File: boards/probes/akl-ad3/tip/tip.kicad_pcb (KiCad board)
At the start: 2 copper layers, 44.5 x 25.5 mm, 11 parts, among them J1 Conn_01x10_shielded, J2 SOCKET, J3 SOCKET

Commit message: v0.2 AKL-AD3 tip
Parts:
- removed the REF** at (118.5, 54.5)
- added REF**: MECHANICAL_CLEARANCEHOLE_M1_UNPLATED, azonenberg_pcb:MECHANICAL_CLEARANCEHOLE_M1_UNPLATED, F.Cu at (118.5, 79.5)
- added REF**: MECHANICAL_CLEARANCEHOLE_M1_UNPLATED, azonenberg_pcb:MECHANICAL_CLEARANCEHOLE_M1_UNPLATED, F.Cu at (118.5, 52.5)
- added REF**: MECHANICAL_CLEARANCEHOLE_M1_UNPLATED, azonenberg_pcb:MECHANICAL_CLEARANCEHOLE_M1_UNPLATED, F.Cu at (120.5, 52.5)
- moved REF** 2.83 mm to (120.5, 79.5)
- moved J2 2.24 mm to (123.2, 52.9)
- moved J3 2.24 mm to (123.2, 79.2)
- moved R1 2.24 mm to (118.8, 54.0)
- moved R2 2.24 mm to (118.8, 78.0)
- moved R3 2.24 mm to (119.8, 54.0)
- moved R4 2.24 mm to (119.8, 78.0)
- moved R5 2.24 mm to (121.0, 54.0)
- moved R6 2.24 mm to (121.0, 78.0)
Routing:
- net /GND: track 195.4 -> 207.4 mm, vias 176 -> 188
- net /IN_R_N: track 48.6 -> 52.1 mm
- net /IN_R_P: track 48.7 -> 51.7 mm
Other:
- board size 44.5 x 25.5 mm -> 45.5 x 29.5 mm
- board text added: "v0.2"
- board text removed: "v0.1"

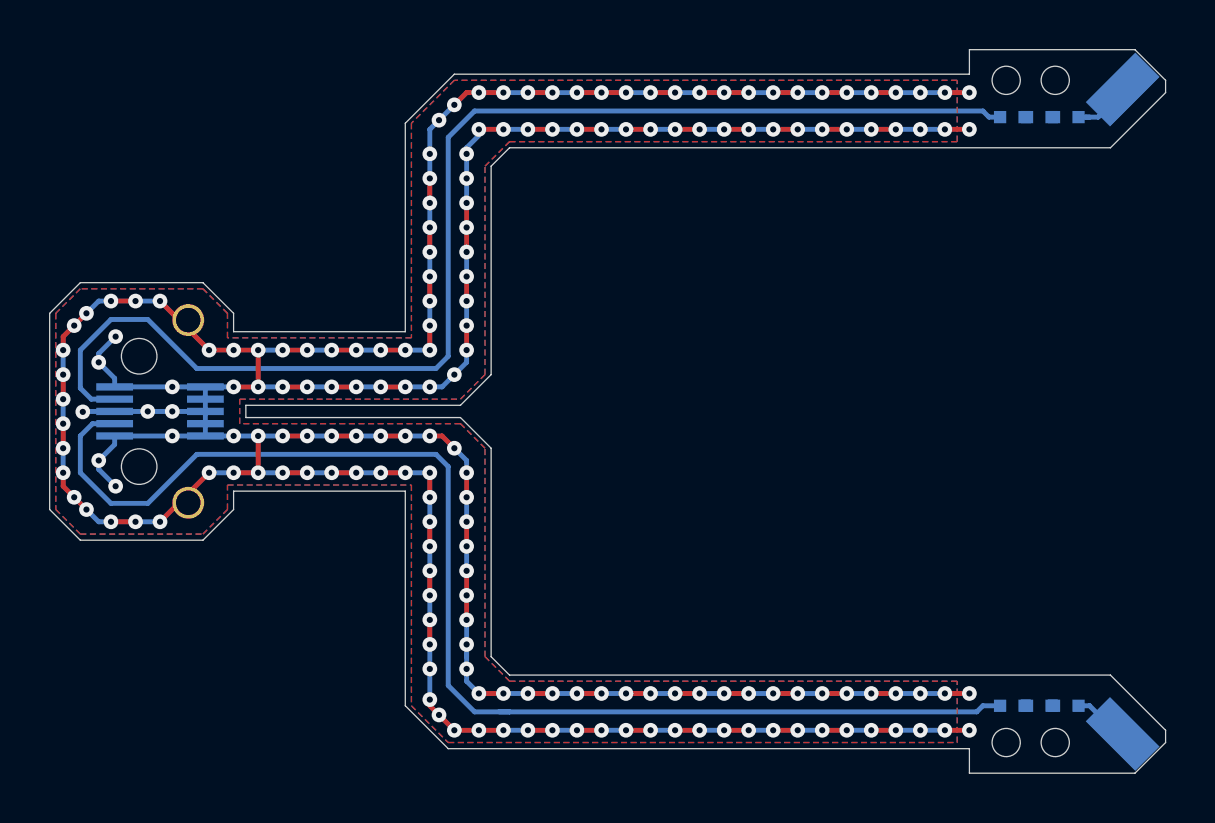
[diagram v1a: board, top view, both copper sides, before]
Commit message: Updated tip with correct copper pours. Bumped version number to v0.3 to disambiguate some mistyped numbers before.
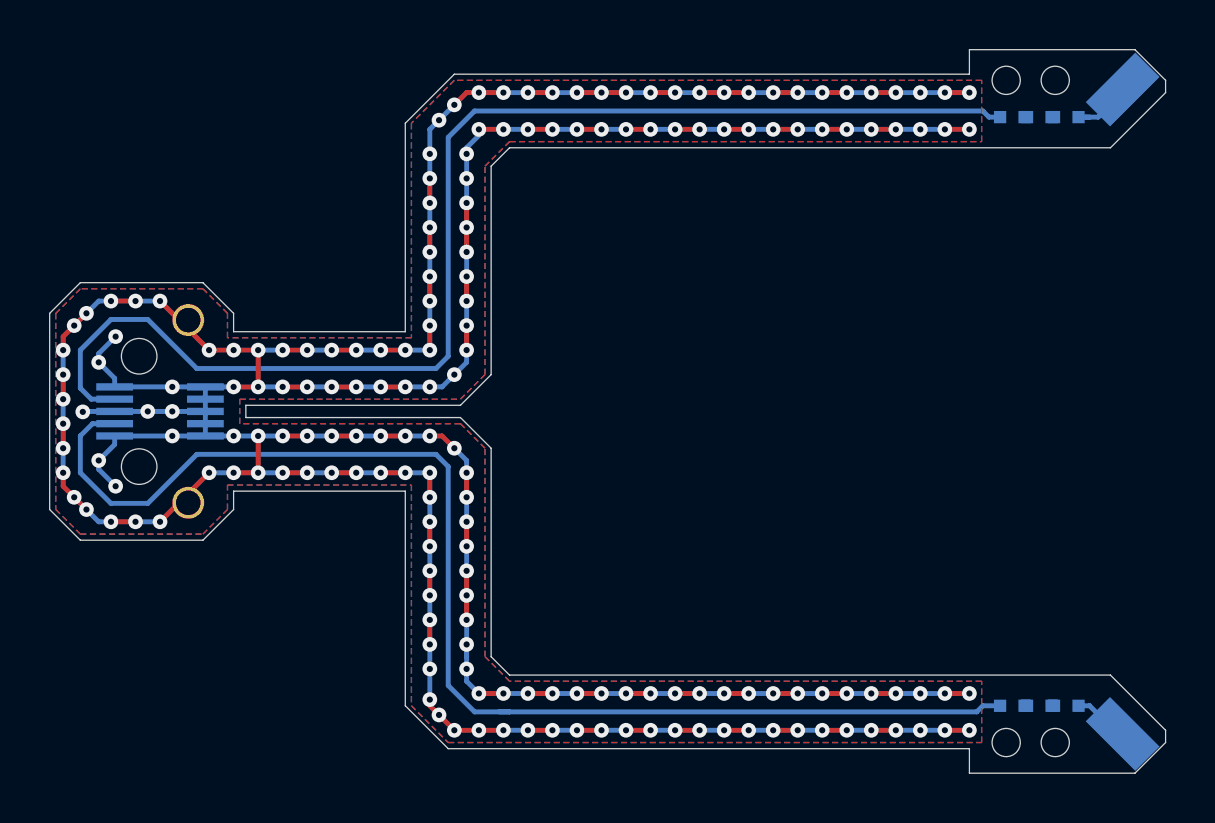
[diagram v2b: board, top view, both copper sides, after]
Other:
- board text added: "v0.3"
- board text removed: "v0.2"
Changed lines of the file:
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@@
     (effects (font (size 0.75 0.75) (thickness 0.1)) (justify mirror))
   )
-  (gr_text v0.2 (at 82.75 62.25) (layer B.SilkS)
+  (gr_text v0.3 (at 82.75 62.25) (layer B.SilkS)
     (effects (font (size 0.75 0.75) (thickness 0.1)) (justify mirror))
   )
@@
         (xy 80.75 61) (xy 79.75 62) (xy 79.75 70) (xy 80.75 71) (xy 85.75 71)
         (xy 86.75 70) (xy 86.75 69) (xy 94.25 69) (xy 94.25 78) (xy 95.75 79.5)
-        (xy 116.5 79.5) (xy 116.5 77) (xy 98.25 77) (xy 97.25 76) (xy 97.25 67.5)
+        (xy 117.5 79.5) (xy 117.5 77) (xy 98.25 77) (xy 97.25 76) (xy 97.25 67.5)
         (xy 96.25 66.5) (xy 87.25 66.5) (xy 87.25 65.5) (xy 96.25 65.5) (xy 97.25 64.5)
-        (xy 97.25 56) (xy 98.25 55) (xy 116.5 55) (xy 116.5 52.5) (xy 96 52.5)
+        (xy 97.25 56) (xy 98.25 55) (xy 117.5 55) (xy 117.5 52.5) (xy 96 52.5)
         (xy 94.25 54.25) (xy 94.25 63) (xy 86.75 63) (xy 86.75 62) (xy 85.75 61)
       )
@@
         (xy 80.75 61) (xy 79.75 62) (xy 79.75 70) (xy 80.75 71) (xy 85.75 71)
         (xy 86.75 70) (xy 86.75 69) (xy 94.25 69) (xy 94.25 78) (xy 95.75 79.5)
-        (xy 116.5 79.5) (xy 116.5 77) (xy 98.25 77) (xy 97.25 76) (xy 97.25 67.5)
+        (xy 117.5 79.5) (xy 117.5 77) (xy 98.25 77) (xy 97.25 76) (xy 97.25 67.5)
         (xy 96.25 66.5) (xy 87.25 66.5) (xy 87.25 65.5) (xy 96.25 65.5) (xy 97.25 64.5)
-        (xy 97.25 56) (xy 98.25 55) (xy 116.5 55) (xy 116.5 52.5) (xy 96 52.5)
+        (xy 97.25 56) (xy 98.25 55) (xy 117.5 55) (xy 117.5 52.5) (xy 96 52.5)
         (xy 94.25 54.25) (xy 94.25 63) (xy 86.75 63) (xy 86.75 62) (xy 85.75 61)
       )

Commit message: Missing change from last commit
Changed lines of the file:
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@@
     (thickness 0.2)
     (drawings 40)
-    (tracks 446)
+    (tracks 444)
     (zones 0)
     (modules 13)
@@
   (segment (start 82 62.25) (end 83.5 62.25) (width 0.2) (layer B.Cu) (net 3))
   (segment (start 117.55 78) (end 118.25 78) (width 0.2) (layer B.Cu) (net 5))
+  (segment (start 96.824998 78.25) (end 117.3 78.25) (width 0.2) (layer B.Cu) (net 5))
+  (segment (start 95.75 77.175002) (end 96.824998 78.25) (width 0.2) (layer B.Cu) (net 5))
+  (segment (start 95.25 67.75) (end 95.75 68.25) (width 0.2) (layer B.Cu) (net 5))
   (segment (start 117.3 78.25) (end 117.55 78) (width 0.2) (layer B.Cu) (net 5))
-  (segment (start 96.824998 78.25) (end 98.25 78.25) (width 0.2) (layer B.Cu) (net 5))
-  (segment (start 95.75 77.175002) (end 96.824998 78.25) (width 0.2) (layer B.Cu) (net 5))
   (segment (start 85.5 67.75) (end 95.25 67.75) (width 0.2) (layer B.Cu) (net 5))
   (segment (start 82 69.75) (end 83.5 69.75) (width 0.2) (layer B.Cu) (net 5))
-  (segment (start 95.25 67.75) (end 95.75 68.25) (width 0.2) (layer B.Cu) (net 5))
-  (segment (start 83.5 69.75) (end 85.5 67.75) (width 0.2) (layer B.Cu) (net 5))
-  (segment (start 98.25 78.25) (end 117.3 78.25) (width 0.2) (layer B.Cu) (net 5))
-  (segment (start 97.824998 78.25) (end 98.25 78.25) (width 0.2) (layer B.Cu) (net 5))
   (segment (start 82.15 66.5) (end 81.25 66.5) (width 0.2) (layer B.Cu) (net 5))
   (segment (start 95.75 68.25) (end 95.75 77.175002) (width 0.2) (layer B.Cu) (net 5))
+  (segment (start 80.75 67) (end 80.75 68.5) (width 0.2) (layer B.Cu) (net 5))
   (segment (start 81.25 66.5) (end 80.75 67) (width 0.2) (layer B.Cu) (net 5))
-  (segment (start 80.75 67) (end 80.75 68.5) (width 0.2) (layer B.Cu) (net 5))
   (segment (start 80.75 68.5) (end 82 69.75) (width 0.2) (layer B.Cu) (net 5))
+  (segment (start 83.5 69.75) (end 85.5 67.75) (width 0.2) (layer B.Cu) (net 5))
   (segment (start 85.85 65) (end 85.85 66.85) (width 0.2) (layer B.Cu) (net 9))
   (segment (start 86 66) (end 85.85 66) (width 0.2) (layer B.Cu) (net 9))
